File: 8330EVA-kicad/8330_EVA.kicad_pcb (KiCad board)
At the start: 2 copper layers, 24 parts, among them J1 USB_B_Micro, U2 FT232H, Y1 12Mhz

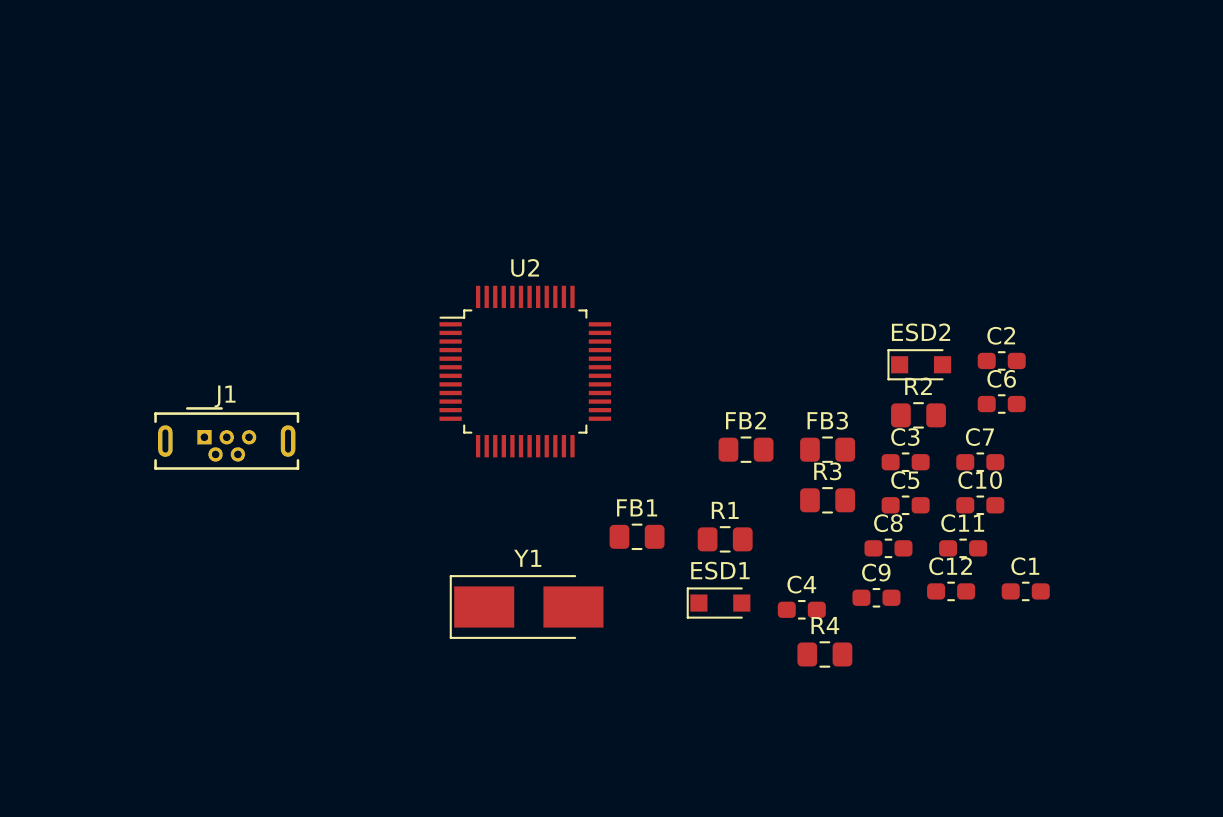
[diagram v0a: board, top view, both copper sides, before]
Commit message: add symbol/package of AD8131 and AD8330
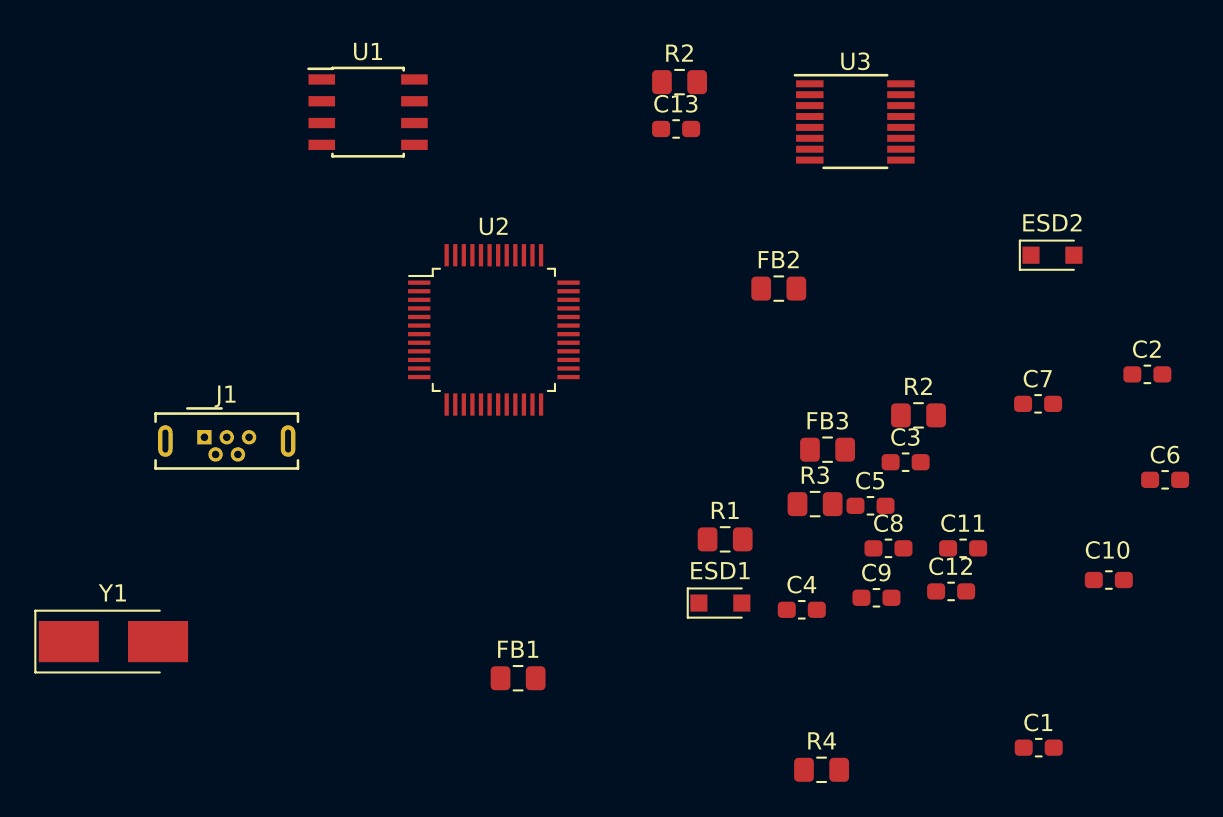
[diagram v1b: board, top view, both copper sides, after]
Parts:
- added C13: 10n, Capacitor_SMD:C_0603_1608Metric_Pad1.05x0.95mm_HandSolder, F.Cu at (144.8, 82.6)
- added R2: 10k, Resistor_SMD:R_0805_2012Metric_Pad1.15x1.40mm_HandSolder, F.Cu at (145.0, 79.8)
- added U1: AD8131, Package_SO:SOIC-8_3.9x4.9mm_P1.27mm, F.Cu at (126.9, 81.6)
- added U3: AD8330, Package_SO:QSOP-16_3.9x4.9mm_P0.635mm, F.Cu at (155.3, 82.2)
- moved Y1 24.3 mm to (112.0, 112.5)
- moved FB1 10.8 mm to (135.6, 114.6)
- moved C6 10.5 mm to (173.3, 103.0)
- moved ESD2 9.97 mm to (166.8, 89.9)
- moved FB2 9.58 mm to (150.8, 91.9)
- moved C1 9.14 mm to (166.0, 118.6)
- moved C10 8.66 mm to (170.0, 108.9)
- moved C2 8.52 mm to (172.3, 96.9)
- moved R4 6.72 mm to (153.3, 119.9)
- moved C7 4.79 mm to (165.9, 98.6)
- moved U2 3.04 mm to (134.2, 94.3)
- moved C5 2.05 mm to (156.2, 104.5)
- moved R3 0.76 mm to (152.9, 104.4)
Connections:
- FB2 pad 1: /USB2SPI/VCC_3V3 -> /USB2SPI/VCCIO
- FB3 pad 1: /USB2SPI/VCC_3V3 -> /USB2SPI/VCCIO
- J1 pad 6: Net-(J1-Pad6) -> Earth
- U2 pad 34: Net-(U2-Pad34) -> /USB2SPI/RST
- U2 pad 39: Net-(U2-Pad39) -> /USB2SPI/VCCIO

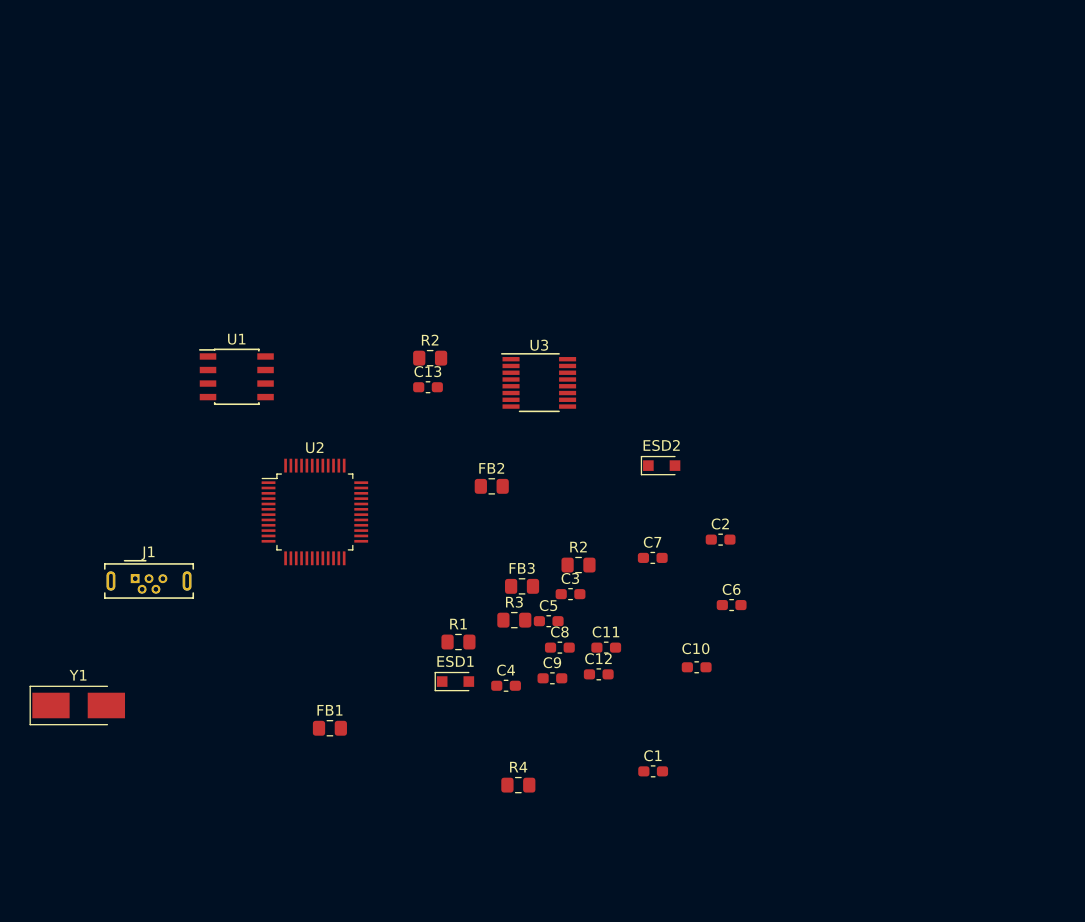
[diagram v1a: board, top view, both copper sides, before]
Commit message: 完成变压器3d模型绘制
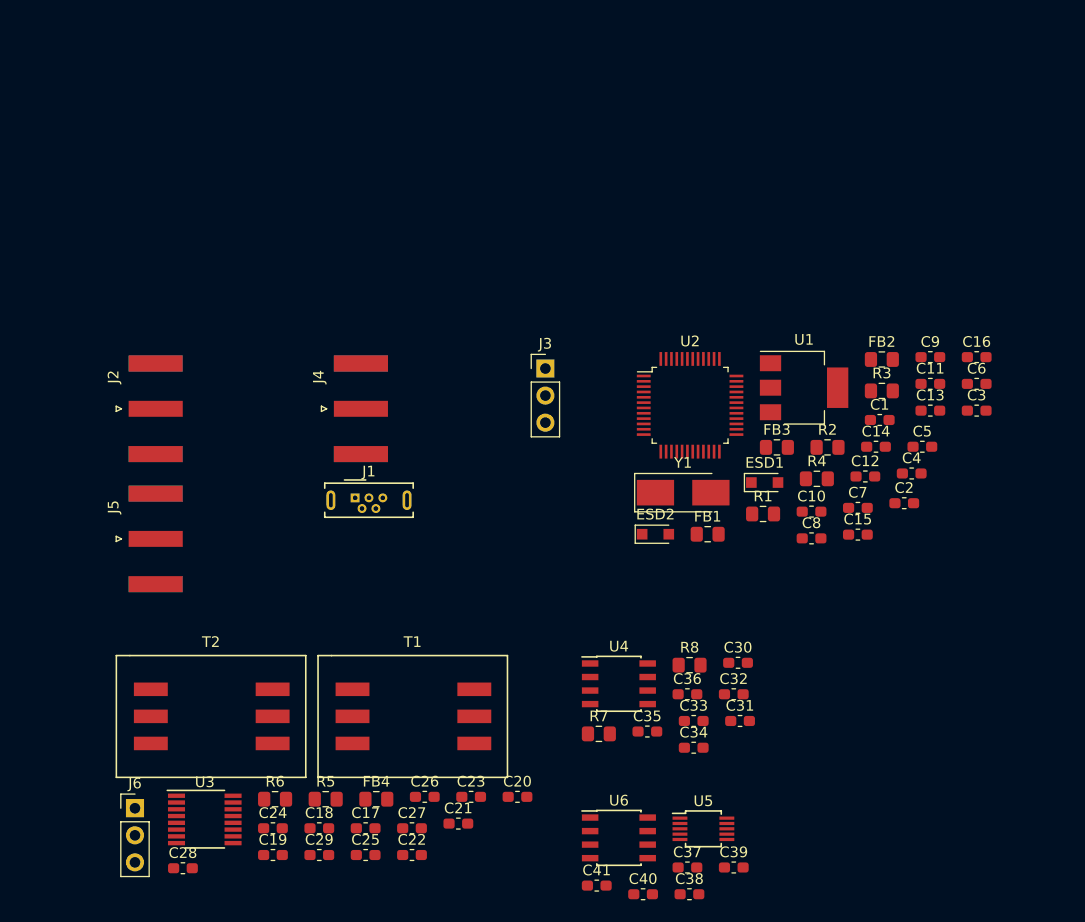
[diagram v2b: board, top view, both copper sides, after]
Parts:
- removed the R2 at (145.0, 79.8)
- removed the R2 at (159.0, 99.3)
- added C14: 4.7u, Capacitor_SMD:C_0603_1608Metric_Pad1.05x0.95mm_HandSolder, F.Cu at (186.9, 88.2)
- added C15: 100n, Capacitor_SMD:C_0603_1608Metric_Pad1.05x0.95mm_HandSolder, F.Cu at (185.2, 96.4)
- added C16: 100n, Capacitor_SMD:C_0603_1608Metric_Pad1.05x0.95mm_HandSolder, F.Cu at (196.3, 79.8)
- added C17: 0.1u, Capacitor_SMD:C_0603_1608Metric_Pad1.05x0.95mm_HandSolder, F.Cu at (139.0, 124.0)
- added C18: 0.1u, Capacitor_SMD:C_0603_1608Metric_Pad1.05x0.95mm_HandSolder, F.Cu at (134.6, 124.0)
- added C19: 0.1u, Capacitor_SMD:C_0603_1608Metric_Pad1.05x0.95mm_HandSolder, F.Cu at (130.3, 126.5)
- added C20: 0.1u, Capacitor_SMD:C_0603_1608Metric_Pad1.05x0.95mm_HandSolder, F.Cu at (153.2, 121.0)
- added C21: 0.1u, Capacitor_SMD:C_0603_1608Metric_Pad1.05x0.95mm_HandSolder, F.Cu at (147.7, 123.5)
- added C22: 0.1u, Capacitor_SMD:C_0603_1608Metric_Pad1.05x0.95mm_HandSolder, F.Cu at (143.3, 126.5)
- added C23: 0.1u, Capacitor_SMD:C_0603_1608Metric_Pad1.05x0.95mm_HandSolder, F.Cu at (148.9, 121.0)
- added C24: 0.1u, Capacitor_SMD:C_0603_1608Metric_Pad1.05x0.95mm_HandSolder, F.Cu at (130.3, 124.0)
- added C25: 1n, Capacitor_SMD:C_0603_1608Metric_Pad1.05x0.95mm_HandSolder, F.Cu at (139.0, 126.5)
- added C26: 12p, Capacitor_SMD:C_0603_1608Metric_Pad1.05x0.95mm_HandSolder, F.Cu at (144.5, 121.0)
- added C27: 12p, Capacitor_SMD:C_0603_1608Metric_Pad1.05x0.95mm_HandSolder, F.Cu at (143.3, 124.0)
- added C28: 0.1u, Capacitor_SMD:C_0603_1608Metric_Pad1.05x0.95mm_HandSolder, F.Cu at (121.8, 127.7)
- added C29: 0.1u, Capacitor_SMD:C_0603_1608Metric_Pad1.05x0.95mm_HandSolder, F.Cu at (134.6, 126.5)
- added C30: 0.1u, Capacitor_SMD:C_0603_1608Metric_Pad1.05x0.95mm_HandSolder, F.Cu at (173.9, 108.4)
- added C31: 0.1u, Capacitor_SMD:C_0603_1608Metric_Pad1.05x0.95mm_HandSolder, F.Cu at (174.1, 113.9)
- added C32: 10u, Capacitor_SMD:C_0603_1608Metric_Pad1.05x0.95mm_HandSolder, F.Cu at (173.5, 111.4)
- added C33: 10n, Capacitor_SMD:C_0603_1608Metric_Pad1.05x0.95mm_HandSolder, F.Cu at (169.8, 113.9)
- added C34: 0.1u, Capacitor_SMD:C_0603_1608Metric_Pad1.05x0.95mm_HandSolder, F.Cu at (169.8, 116.4)
- added C35: 10u, Capacitor_SMD:C_0603_1608Metric_Pad1.05x0.95mm_HandSolder, F.Cu at (165.4, 114.9)
- added C36: 10n, Capacitor_SMD:C_0603_1608Metric_Pad1.05x0.95mm_HandSolder, F.Cu at (169.2, 111.4)
- added C37: 1u, Capacitor_SMD:C_0603_1608Metric_Pad1.05x0.95mm_HandSolder, F.Cu at (169.2, 127.7)
- added C38: 1u, Capacitor_SMD:C_0603_1608Metric_Pad1.05x0.95mm_HandSolder, F.Cu at (169.4, 130.2)
- added C39: 0.1u, Capacitor_SMD:C_0603_1608Metric_Pad1.05x0.95mm_HandSolder, F.Cu at (173.5, 127.7)
- added C40: 10u, Capacitor_SMD:C_0603_1608Metric_Pad1.05x0.95mm_HandSolder, F.Cu at (165.0, 130.2)
- added C41: 0.1u, Capacitor_SMD:C_0603_1608Metric_Pad1.05x0.95mm_HandSolder, F.Cu at (160.7, 129.4)
- added FB4: Ferrite_Bead, Inductor_SMD:L_0805_2012Metric_Pad1.15x1.40mm_HandSolder, F.Cu at (140.0, 121.2)
- added J2: Conn_Coaxial, Connector_Coaxial:SMA_Amphenol_132289_EdgeMount, F.Cu at (119.3, 84.6)
- added J3: Conn_01x03_Male, Connector_PinHeader_2.54mm:PinHeader_1x03_P2.54mm_Vertical, F.Cu at (155.8, 80.8)
- added J4: Conn_Coaxial, Connector_Coaxial:SMA_Amphenol_132289_EdgeMount, F.Cu at (138.5, 84.6)
- added J5: Conn_Coaxial, Connector_Coaxial:SMA_Amphenol_132289_EdgeMount, F.Cu at (119.3, 96.8)
- added J6: Conn_01x03_Male, Connector_PinHeader_2.54mm:PinHeader_1x03_P2.54mm_Vertical, F.Cu at (117.3, 122.1)
- added R2: 10k, Resistor_SMD:R_0805_2012Metric_Pad1.15x1.40mm_HandSolder, F.Cu at (182.3, 88.2)
- added R5: 0, Resistor_SMD:R_0805_2012Metric_Pad1.15x1.40mm_HandSolder, F.Cu at (135.2, 121.2)
- added R6: 1k, Resistor_SMD:R_0805_2012Metric_Pad1.15x1.40mm_HandSolder, F.Cu at (130.5, 121.2)
- added R7: 49.9, Resistor_SMD:R_0805_2012Metric_Pad1.15x1.40mm_HandSolder, F.Cu at (160.9, 115.1)
- added R8: 24.9, Resistor_SMD:R_0805_2012Metric_Pad1.15x1.40mm_HandSolder, F.Cu at (169.4, 108.7)
- added T1: T1-1T-KK81, 8330EVA-footprint-extra:Mini_Circuit_RF_Transformer_SO6, F.Cu at (143.3, 114.1)
- added T2: T1-1T-KK81, 8330EVA-footprint-extra:Mini_Circuit_RF_Transformer_SO6, F.Cu at (124.4, 114.1)
- added U4: AD8131, Package_SO:SOIC-8_3.9x4.9mm_P1.27mm, F.Cu at (162.7, 110.4)
- added U5: AD5312, Package_SO:MSOP-10_3x3mm_P0.5mm, F.Cu at (170.7, 124.0)
- added U6: REF192, Package_SO:SOIC-8_3.9x4.9mm_P1.27mm, F.Cu at (162.7, 124.9)
- U1: value AD8131 -> AMS1117-3.3; footprint Package_SO:SOIC-8_3.9x4.9mm_P1.27mm -> Package_TO_SOT_SMD:SOT-223-3_TabPin2
- moved Y1 60.1 mm to (168.8, 92.5)
- moved U1 53.3 mm to (180.1, 82.6)
- moved U3 51.6 mm to (123.9, 123.1)
- moved C13 47.2 mm to (192.0, 84.8)
- moved C9 46.5 mm to (192.0, 79.8)
- moved C4 43.0 mm to (190.2, 90.7)
- moved C3 41.8 mm to (196.3, 84.8)
- moved R3 40.7 mm to (187.4, 82.9)
- moved R4 40.1 mm to (181.3, 91.2)
- moved FB1 39.9 mm to (171.1, 96.4)
- moved C1 39.2 mm to (187.2, 85.7)
- moved C11 39.2 mm to (192.0, 82.3)
- moved C5 38.7 mm to (191.2, 88.2)
- moved FB2 38.5 mm to (187.4, 80.0)
- moved U2 36.6 mm to (169.4, 84.3)
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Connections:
- net Net-(ESD1-Pad1) renamed /USB2SPI/USB_D+
- net Net-(ESD2-Pad1) renamed /USB2SPI/USB_D-
- C1 pad 1: Earth -> /USB2SPI/Ground
- C10 pad 2: Earth -> /USB2SPI/Ground
- C11 pad 2: Earth -> /USB2SPI/Ground
- C12 pad 2: Earth -> /USB2SPI/Ground
- C13 pad 2: Earth -> /USB2SPI/Ground
- C2 pad 2: Earth -> /USB2SPI/Ground
- C3 pad 2: Earth -> /USB2SPI/Ground
- C4 pad 2: Earth -> /USB2SPI/Ground
- C5 pad 2: Earth -> /USB2SPI/Ground
- C6 pad 2: Earth -> /USB2SPI/Ground
- C7 pad 2: Earth -> /USB2SPI/Ground
- C8 pad 2: Earth -> /USB2SPI/Ground
- C9 pad 2: Earth -> /USB2SPI/Ground
- ESD1 pad 2: Earth -> /USB2SPI/Ground
- ESD2 pad 2: Earth -> /USB2SPI/Ground
- J1 pad 1: Net-(C1-Pad2) -> /USB2SPI/VBUS
- J1 pad 5: Earth -> /USB2SPI/Ground
- J1 pad 6: Earth -> /USB2SPI/Ground
- R1 pad 2: Earth -> /USB2SPI/Ground
- U1 pad 1: Net-(U1-Pad1) -> /USB2SPI/Ground
- U1 pad 2: Net-(U1-Pad2) -> /USB2SPI/VCCIO
- U1 pad 3: Net-(U1-Pad3) -> /DAC/VCC_+5V
- U2 pad 10: Earth -> /USB2SPI/Ground
- U2 pad 11: Earth -> /USB2SPI/Ground
- U2 pad 22: Earth -> /USB2SPI/Ground
- U2 pad 23: Earth -> /USB2SPI/Ground
- U2 pad 35: Earth -> /USB2SPI/Ground
- U2 pad 36: Earth -> /USB2SPI/Ground
- U2 pad 4: Earth -> /USB2SPI/Ground
- U2 pad 40: /USB2SPI/VBUS -> /USB2SPI/VCCIO
- U2 pad 41: Earth -> /USB2SPI/Ground
- U2 pad 42: Net-(U2-Pad42) -> /USB2SPI/Ground
- U2 pad 47: Earth -> /USB2SPI/Ground
- U2 pad 48: Earth -> /USB2SPI/Ground
- U2 pad 9: Earth -> /USB2SPI/Ground
- U3 pad 10: Net-(U3-Pad10) -> /DAC/ChannelB
- U3 pad 11: Net-(U3-Pad11) -> Earth
- U3 pad 14: Net-(U3-Pad14) -> /DAC/VCC_+5V
- U3 pad 15: Net-(U3-Pad15) -> /VCA/CNTR
- U3 pad 16: Net-(U3-Pad16) -> /DAC/VCC_+5V
- U3 pad 3: Net-(U3-Pad3) -> /DAC/VCC_+5V
- U3 pad 6: Net-(U3-Pad6) -> Earth
- U3 pad 7: Net-(U3-Pad7) -> /DAC/ChannelA
- U3 pad 9: Net-(U3-Pad9) -> Earth

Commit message: 更新3d模型，替换SMA接头的封装
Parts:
- J2: footprint Connector_Coaxial:SMA_Amphenol_132289_EdgeMount -> Connector_Coaxial:SMA_Amphenol_132134-14_Vertical
- J4, J5: footprint Connector_Coaxial:SMA_Amphenol_132289_EdgeMount -> Connector_Coaxial:SMA_Amphenol_132134-11_Vertical
- moved J4 21.5 mm to (117.2, 81.7)
- moved T1 19.6 mm to (123.9, 111.4)
- moved T2 18.6 mm to (142.8, 111.4)
- moved J2 16.9 mm to (135.9, 81.7)
- moved J5 16.8 mm to (126.6, 81.7)
